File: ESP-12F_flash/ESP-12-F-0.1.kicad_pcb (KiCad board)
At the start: 2 copper layers, 44.2 x 43.4 mm, 9 parts, among them P1 CONN_01X12, P2 CONN_01X02, P3 CONN_01X04, P4 CONN_01X03, U1 ESP-12F

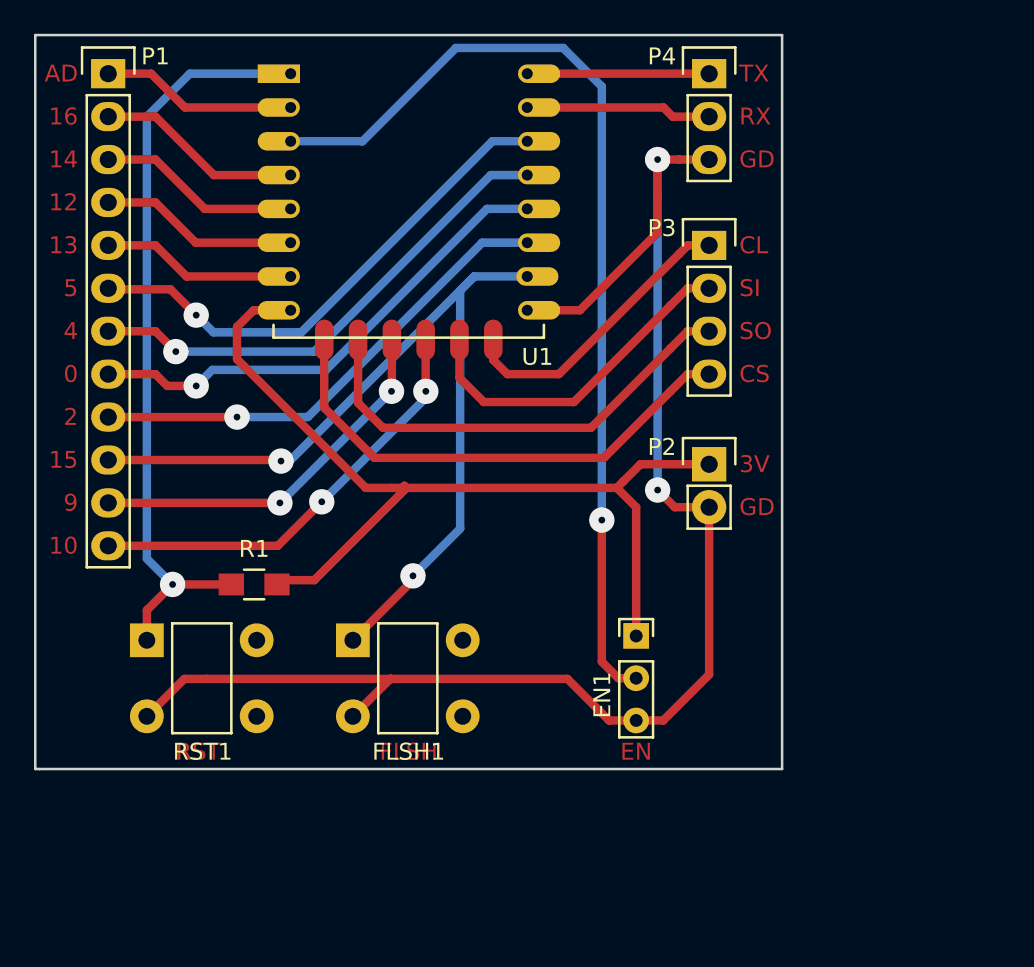
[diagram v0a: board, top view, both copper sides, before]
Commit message: Add missing pull-down/pull-up resistors and remove useless EN switch
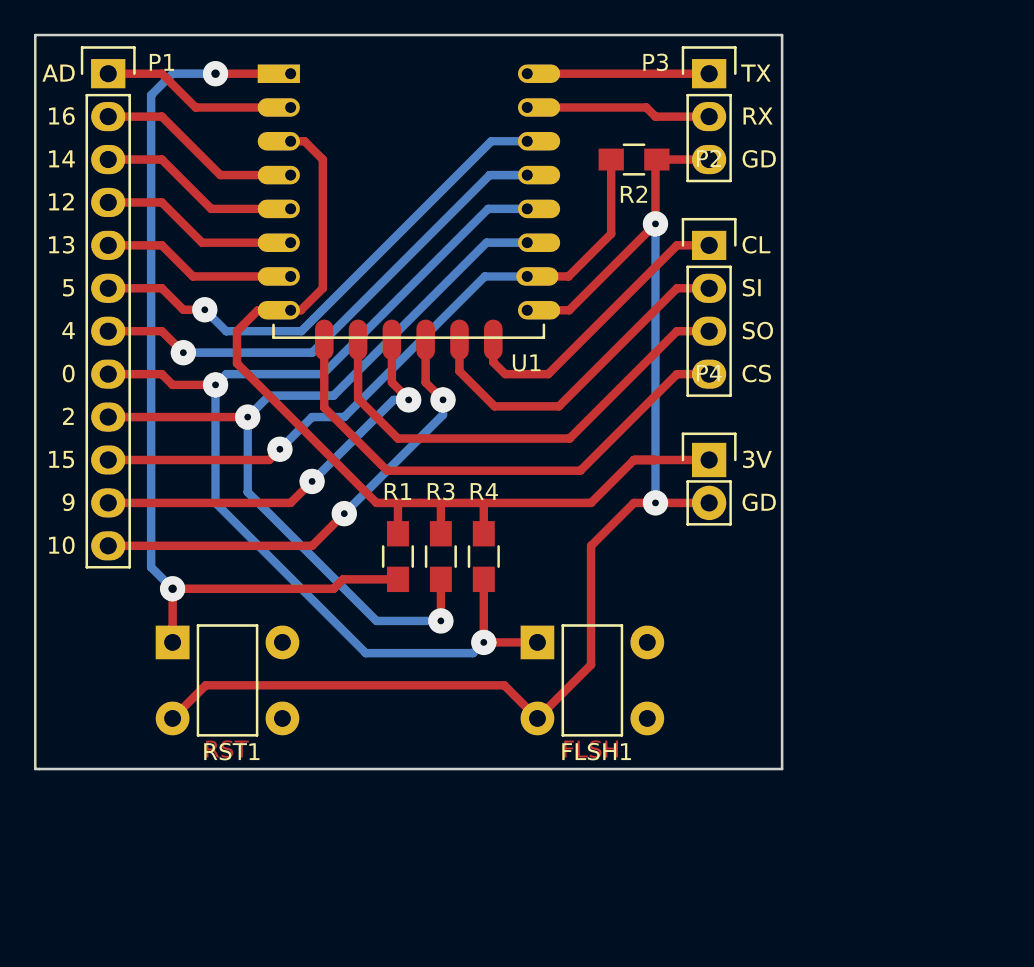
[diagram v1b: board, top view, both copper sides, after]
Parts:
- removed EN1: SPDT, scintilla-components:EG1218
- added R2: 10k, Resistors_SMD:R_0805_HandSoldering, F.Cu at (148.0, 73.7)
- added R3: 10k, Resistors_SMD:R_0805_HandSoldering, F.Cu at (136.5, 97.2)
- added R4: 10k, Resistors_SMD:R_0805_HandSoldering, F.Cu at (139.1, 97.2)
- P1: value CONN_01X12 -> GPIO
- P2: value CONN_01X02 -> SPI; footprint Pin_Headers:Pin_Header_Straight_1x02 -> Pin_Headers:Pin_Header_Straight_1x04
- P3: value CONN_01X04 -> UART; footprint Pin_Headers:Pin_Header_Straight_1x04 -> Pin_Headers:Pin_Header_Straight_1x03
- P4: value CONN_01X03 -> PWR; footprint Pin_Headers:Pin_Header_Straight_1x03 -> Pin_Headers:Pin_Header_Straight_1x02
- moved P4 22.9 mm to (152.4, 91.4)
- moved P2 13.0 mm to (152.4, 78.7)
- moved FLSH1 10.9 mm to (142.2, 102.2)
- moved P3 10.2 mm to (152.4, 68.6)
- moved R1 8.67 mm to (134.0, 97.2), turned to 270 degrees
- moved RST1 1.53 mm to (120.7, 102.2)
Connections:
- FLSH1 pad 1: /GPIO15 -> /GPIO0
- P2 pad 1: +3V3 -> /SCLK
- P2 pad 2: GND -> /MOSI
- P3 pad 1: /SCLK -> /TX
- P3 pad 2: /MOSI -> /RX
- P3 pad 3: /MISO -> GND
- P4 pad 1: /TX -> +3V3
- P4 pad 2: /RX -> GND
- R1 pad 1: Net-(R1-Pad1) -> +3V3
- R1 pad 2: +3V3 -> Net-(R1-Pad2)
- RST1 pad 1: Net-(R1-Pad1) -> Net-(R1-Pad2)
- U1 pad 1: Net-(R1-Pad1) -> Net-(R1-Pad2)
- U1 pad 3: Net-(EN1-Pad2) -> +3V3
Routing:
- net Net-(EN1-Pad2): track 58.1 -> 0.00 mm, vias 1 -> 0
- net Net-(R1-Pad2): track 0.00 -> 55.3 mm, vias 0 -> 2
- net Net-(R1-Pad1): track 45.3 -> 0.00 mm, vias 1 -> 0
- net /GPIO0: track 29.4 -> 63.1 mm, vias 1 -> 2
- net /GPIO2: track 29.1 -> 50.6 mm, vias 1 -> 2
- net /GPIO15: track 53.8 -> 39.7 mm, vias 2 -> 1
- net GND: track 89.5 -> 76.0 mm
- net /GPIO10: track 25.9 -> 27.9 mm
- net +3V3: track 56.6 -> 58.4 mm
- net /GPIO9: track 22.6 -> 24.3 mm
- net /MOSI: track 21.6 -> 20.4 mm
- net /GPIO13: track 12.5 -> 11.6 mm
- net /CSO: track 30.1 -> 30.7 mm
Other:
- net class Default: via_drill 0.4 -> 0.5
- board text removed: "EN"

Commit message: Update ESP-12-F flash breakout to isolate I2C pins
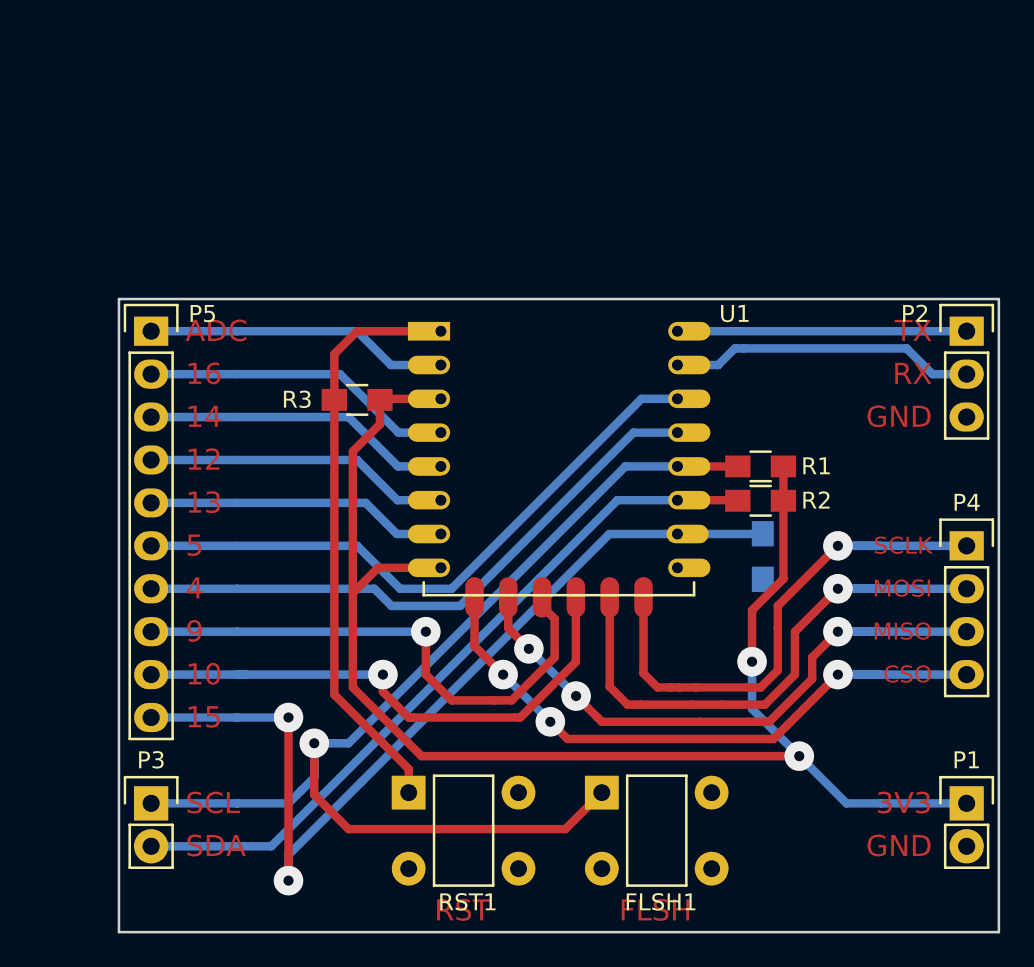
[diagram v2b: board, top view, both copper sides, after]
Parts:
- added P5: GPIO_CONN, Pin_Headers:Pin_Header_Straight_1x10, F.Cu at (119.4, 83.8)
- FLSH1, RST1: footprint scintilla-components:1825910-6 -> scintilla:1825910-6
- P1: value GPIO -> PWR_CONN; footprint Pin_Headers:Pin_Header_Straight_1x12 -> Pin_Headers:Pin_Header_Straight_1x02
- P2: value SPI -> UART_BUS; footprint Pin_Headers:Pin_Header_Straight_1x04 -> Pin_Headers:Pin_Header_Straight_1x03
- P3: value UART -> I2C_BUS; footprint Pin_Headers:Pin_Header_Straight_1x03 -> Pin_Headers:Pin_Header_Straight_1x02
- P4: value PWR -> SPI_BUS; footprint Pin_Headers:Pin_Header_Straight_1x02 -> Pin_Headers:Pin_Header_Straight_1x04
- R1, R2: value 10k -> 4k7
- R4: moved to B.Cu
- U1: footprint ESP8266:ESP-12F -> scintilla:ESP-12F
- moved P1 66.7 mm to (167.6, 111.8)
- moved P3 54.4 mm to (119.4, 111.8)
- moved R1 22.1 mm to (155.4, 91.8), turned to 180 degrees
- moved R2 21.5 mm to (155.4, 93.9)
- moved U1 17.6 mm to (136.5, 83.8)
- moved RST1 16.6 mm to (134.6, 111.1)
- moved R4 16.5 mm to (155.6, 97.2)
- moved P2 16.1 mm to (167.6, 83.8)
- moved P4 16.1 mm to (167.6, 96.5)
- moved R3 10.5 mm to (131.6, 87.9), turned to 180 degrees
- moved FLSH1 9.67 mm to (146.1, 111.1)
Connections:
- FLSH1 pad 1: /GPIO0 -> /SCL
- P1 pad 1: /ADC -> +3V3
- P1 pad 2: /GPIO16 -> GND
- P2 pad 1: /SCLK -> /TX
- P2 pad 2: /MOSI -> /RX
- P2 pad 3: /MISO -> GND
- P3 pad 1: /TX -> /SCL
- P3 pad 2: /RX -> /SDA
- P4 pad 1: +3V3 -> /SCLK
- P4 pad 2: GND -> /MOSI
- R1 pad 2: Net-(R1-Pad2) -> /SCL
- R2 pad 1: GND -> +3V3
- R2 pad 2: /GPIO15 -> /SDA
- R3 pad 2: /GPIO2 -> /RESET
- R4 pad 1: +3V3 -> /GPIO15
- R4 pad 2: /GPIO0 -> GND
- RST1 pad 1: Net-(R1-Pad2) -> /RESET
- U1 pad 1: Net-(R1-Pad2) -> /RESET
- U1 pad 17: /GPIO2 -> /SDA
- U1 pad 18: /GPIO0 -> /SCL
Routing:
- net GND: track 76.0 -> 0.00 mm, vias 2 -> 0
- net /SCL: track 0.00 -> 66.0 mm, vias 0 -> 1
- net /GPIO0: track 63.1 -> 0.00 mm, vias 2 -> 0
- net Net-(R1-Pad2): track 55.3 -> 0.00 mm, vias 2 -> 0
- net /GPIO2: track 50.6 -> 0.00 mm, vias 2 -> 0
- net /SDA: track 0.00 -> 43.3 mm
- net /RESET: track 0.00 -> 34.9 mm
- net +3V3: track 58.4 -> 85.5 mm, vias 0 -> 2
- net /GPIO15: track 39.7 -> 55.2 mm, vias 1 -> 2
- net /SCLK: track 18.2 -> 32.2 mm, vias 0 -> 1
- net /MOSI: track 20.4 -> 33.7 mm, vias 0 -> 1
- net /MISO: track 27.9 -> 37.0 mm, vias 0 -> 3
- net /CSO: track 30.7 -> 38.4 mm, vias 0 -> 3
- net /GPIO9: track 24.3 -> 32.0 mm, vias 2 -> 1
- net /RX: track 11.0 -> 18.2 mm
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- added copper zone on B.Cu, net GND
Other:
- board size 44.2 x 43.4 mm -> 52.1 x 37.5 mm
- net class Default: via_dia 1.5 -> 1.75; via_drill 0.5 -> 0.6
- board text added: "3V3"
- board text added: "ADC"
- board text added: "CSO"
- board text added: "GND"
- board text added: "MISO"
- board text added: "MOSI"
- board text added: "SCL"
- board text added: "SCLK"
- board text added: "SDA"
- board text removed: "0"
- board text removed: "2"
- board text removed: "3V"
- board text removed: "AD"
- board text removed: "CL"
- board text removed: "CS"
- board text removed: "GD"
- board text removed: "SI"
- board text removed: "SO"
